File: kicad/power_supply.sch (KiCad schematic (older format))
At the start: 29 parts, among them J5 USB_A_stacked, Q5 BSS83P, Q6 BSS83P, U4 D1213A-04SO, U5 AP2210-3.3, U9 LMR33630

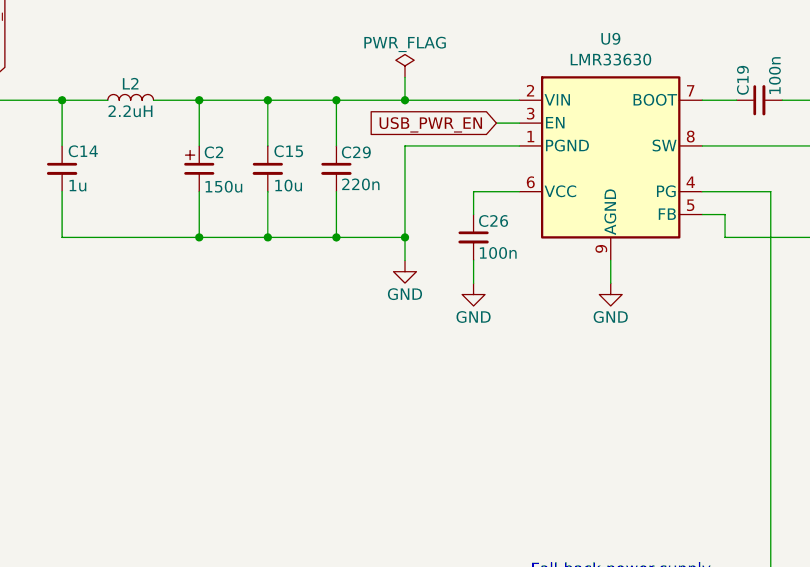
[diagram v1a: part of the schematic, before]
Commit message: Small adjustments after testing
- MOSFET gate driver changed to reduce switch node ringing
- Current measurement output filter time constant reduced to have less delay
- BTN pin allows starting the bootloader if pulled to 3V3 before startup
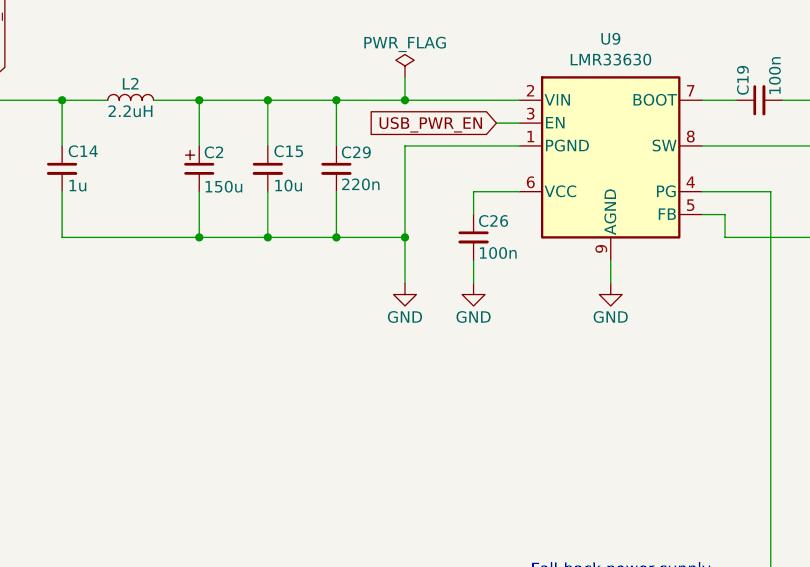
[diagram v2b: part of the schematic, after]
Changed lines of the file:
@@
 encoding utf-8
 Sheet 4 4
-Title "10A MPPT Charge Controller with USB"
-Date "2019-06-03"
-Rev "0.6.1"
-Comp "Libre Solar / Connected Energy"
+Title "MPPT 1210 HUS"
+Date "2019-07-24"
+Rev "0.7.1"
+Comp "Libre Solar"
 Comment1 "Author: Martin Jäger"
 Comment2 "Website: https://libre.solar"
@@
 L power:GND #PWR043
 U 1 1 58C30106
-P 4300 2600
-F 0 "#PWR043" H 4300 2350 50  0001 C CNN
-F 1 "GND" H 4300 2450 50  0000 C CNN
-F 2 "" H 4300 2600 50  0000 C CNN
-F 3 "" H 4300 2600 50  0000 C CNN
-	1    4300 2600
+P 4300 2700
+F 0 "#PWR043" H 4300 2450 50  0001 C CNN
+F 1 "GND" H 4300 2550 50  0000 C CNN
+F 2 "" H 4300 2700 50  0000 C CNN
+F 3 "" H 4300 2700 50  0000 C CNN
+	1    4300 2700
 	1    0    0    -1
 $EndComp
@@
 	4300 2100 4300 2500
 Wire Wire Line
-	4300 2500 4300 2600
+	4300 2500 4300 2700
 Connection ~ 4300 2500
 Wire Wire Line
